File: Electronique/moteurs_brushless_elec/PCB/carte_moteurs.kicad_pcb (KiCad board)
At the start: 2 copper layers, 75 parts, among them J1 CONN_SERIAL, J2 swdio, J3 FAN, K1 Maxon-200142, K2 Maxon-200142, P1 CONN_I2C, P2 CONN_FREE, P3 CONN_CAN, P4 encoder_2, P5 encoder_1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

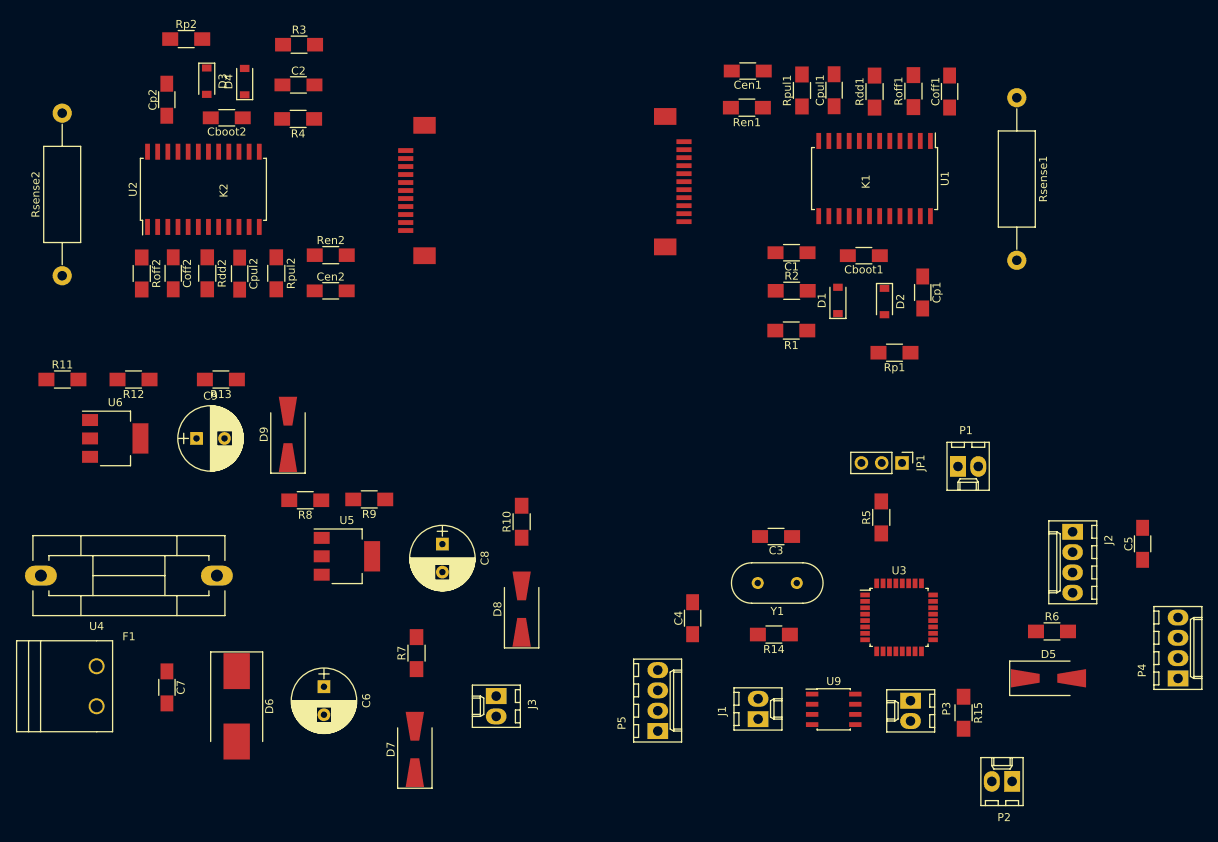
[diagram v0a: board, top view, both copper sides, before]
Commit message: debut routage brushless
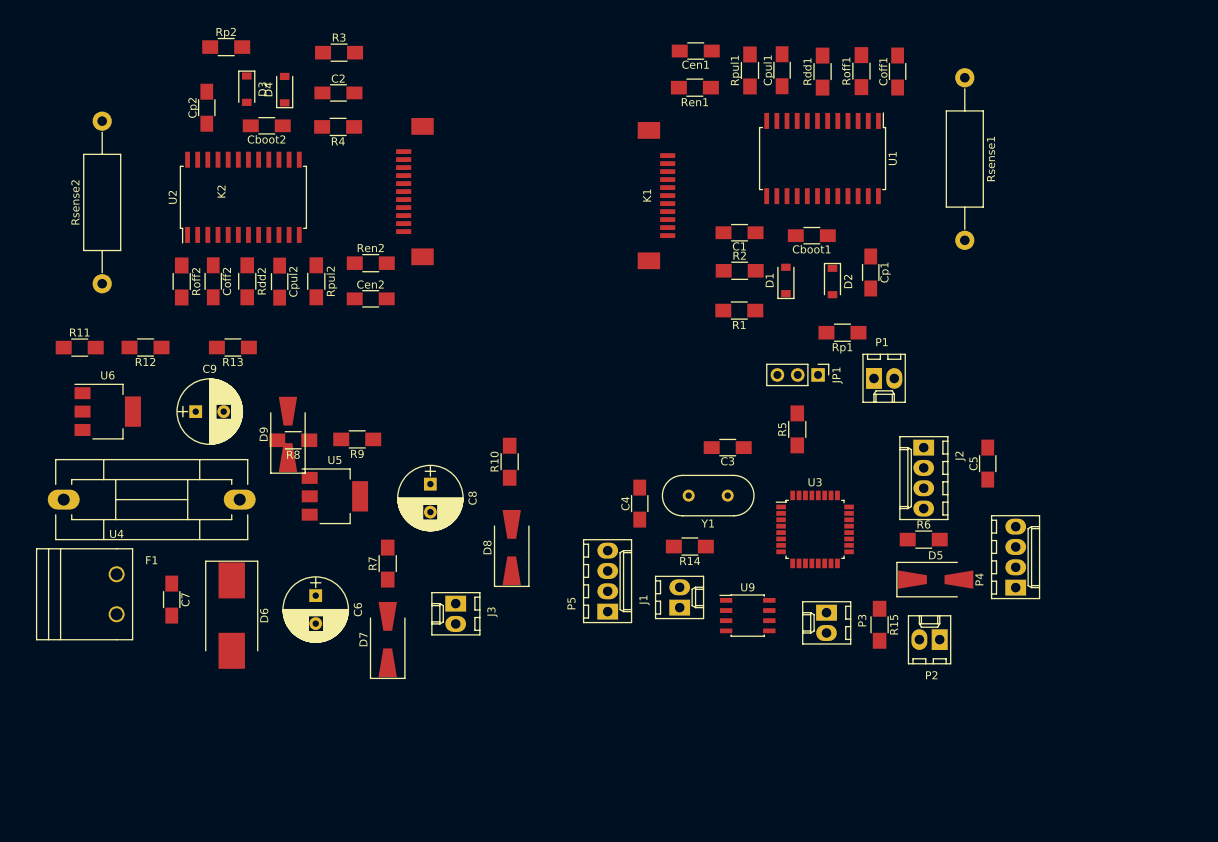
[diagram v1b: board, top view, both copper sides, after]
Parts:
- moved P4 23.3 mm to (140.5, 120.5)
- moved C5 21.8 mm to (137.0, 105.0)
- moved J2 21.4 mm to (129.0, 103.0)
- moved P2 19.9 mm to (131.0, 127.0)
- moved R6 19.7 mm to (129.0, 114.5)
- moved D5 18.7 mm to (130.5, 119.5)
- moved J1 17.0 mm to (98.5, 123.0)
- moved P5 16.2 mm to (89.5, 123.5)
- moved U9 15.9 mm to (107.0, 124.0)
- moved C4 15.8 mm to (93.5, 110.0)
- moved P1 15.2 mm to (122.8, 94.4)
- moved JP1 15.2 mm to (115.8, 93.9)
- moved P3 15.2 mm to (116.9, 123.6)
- moved R14 15.2 mm to (99.8, 115.4)
- moved R5 15.2 mm to (113.2, 100.7)
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
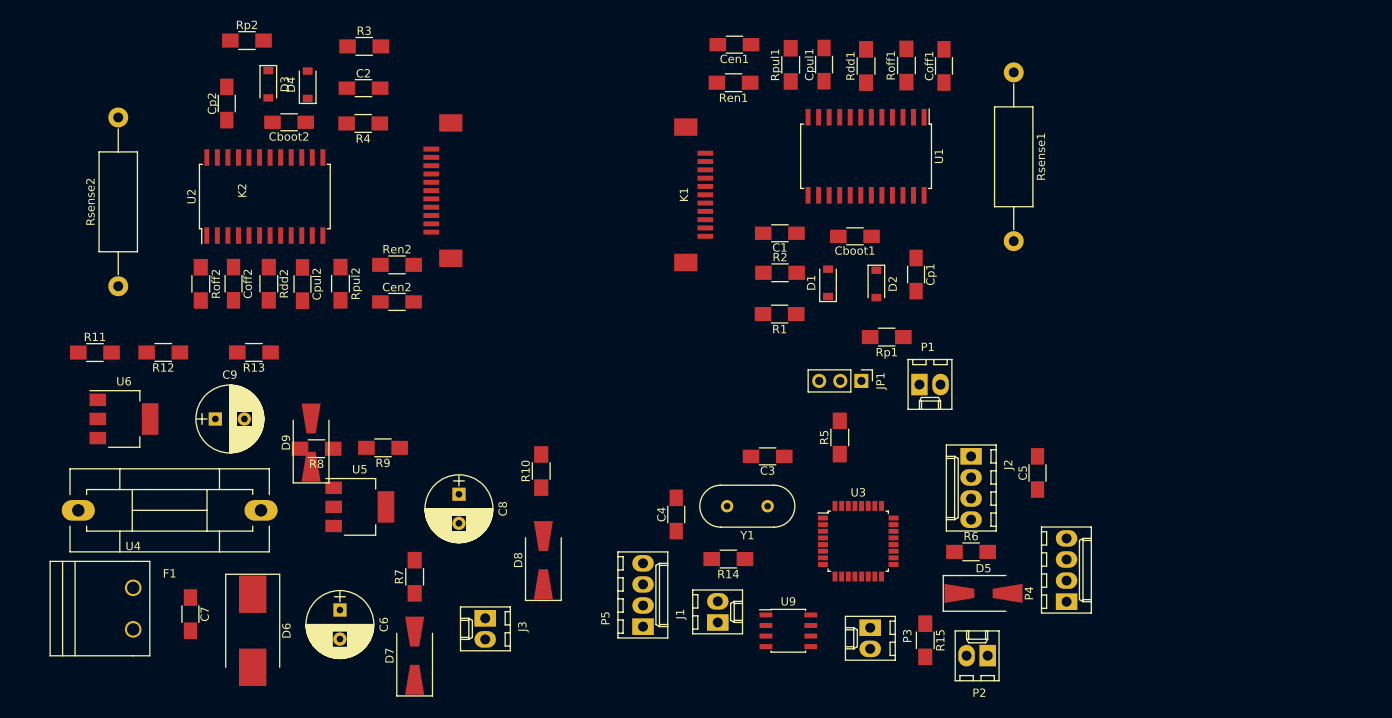
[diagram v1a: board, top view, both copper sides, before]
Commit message: placement brushless
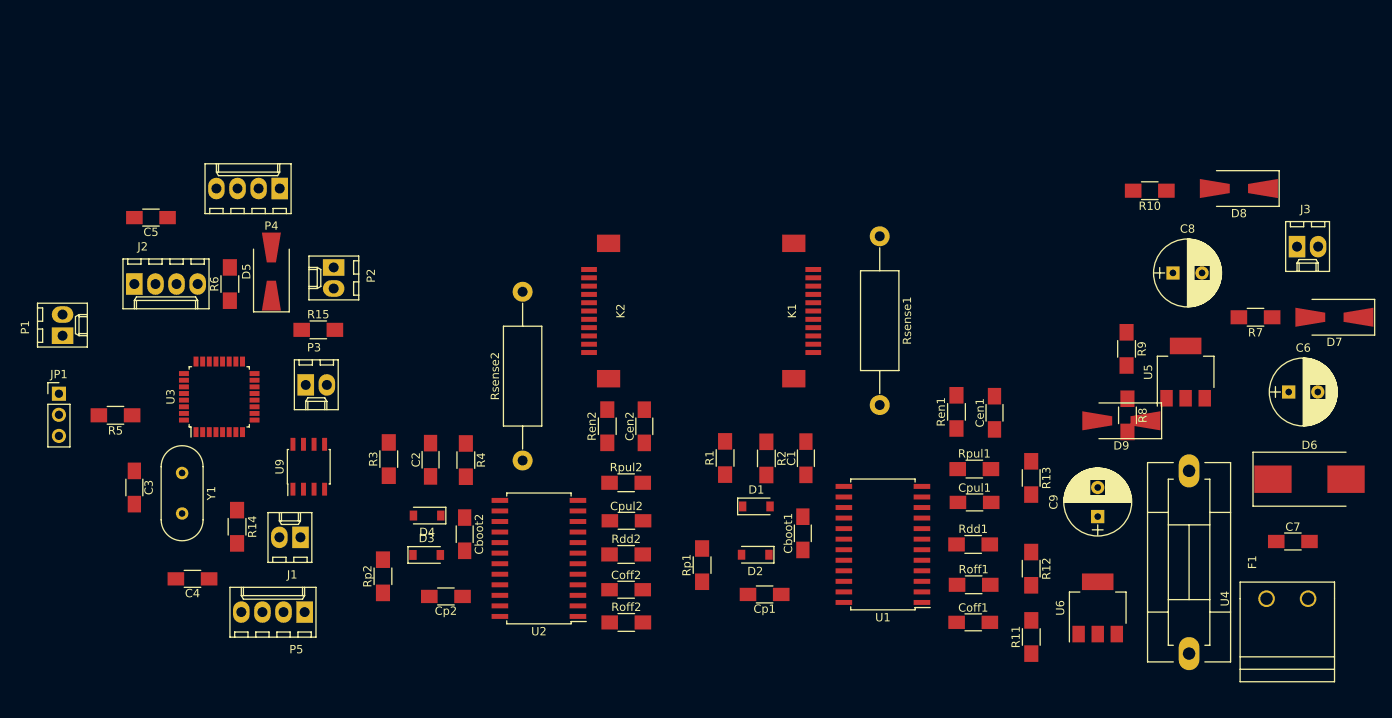
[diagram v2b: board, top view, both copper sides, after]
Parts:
- moved U4 139.0 mm to (167.1, 120.1), turned to 90 degrees
- moved C7 133.0 mm to (167.8, 113.2), turned to 0 degrees
- moved D6 128.6 mm to (169.8, 105.8), turned to 0 degrees
- moved U6 119.4 mm to (144.2, 121.2), turned to 90 degrees
- moved D7 118.0 mm to (172.8, 86.2), turned to 180 degrees
- moved R11 117.8 mm to (136.2, 124.8), turned to 90 degrees
- moved C6 117.2 mm to (167.2, 95.2), turned to 0 degrees
- moved F1 111.9 mm to (155.2, 104.8), turned to 270 degrees
- moved C5 111.1 mm to (30.2, 74.2), turned to 180 degrees
- moved R12 107.7 mm to (136.2, 116.5), turned to 270 degrees
- moved J3 107.5 mm to (168.2, 77.8), turned to 0 degrees
- moved P4 107.0 mm to (45.8, 70.8), turned to 180 degrees
- moved C9 106.9 mm to (144.2, 110.2), turned to 90 degrees
- moved R7 106.0 mm to (163.2, 86.2), turned to 180 degrees
- moved P1 103.3 mm to (19.6, 88.5), turned to 90 degrees
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
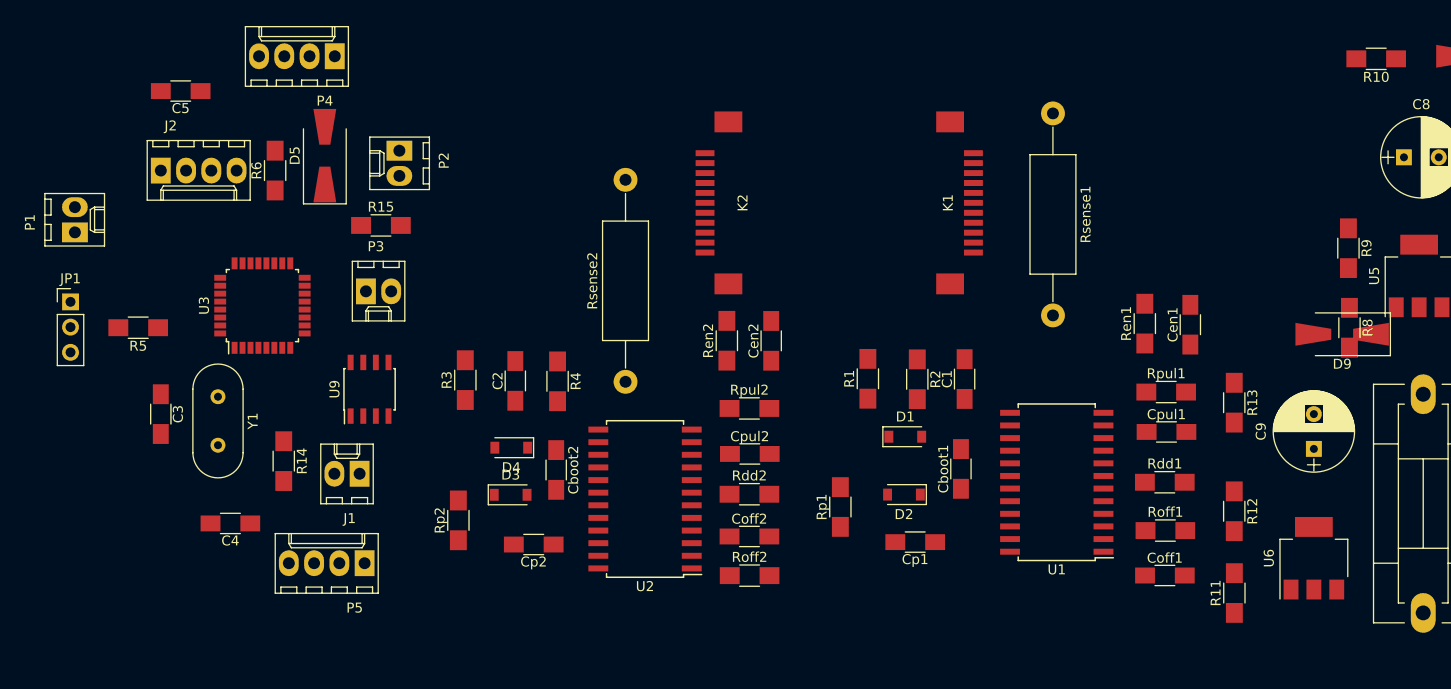
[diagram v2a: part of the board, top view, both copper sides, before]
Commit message: placement brushless
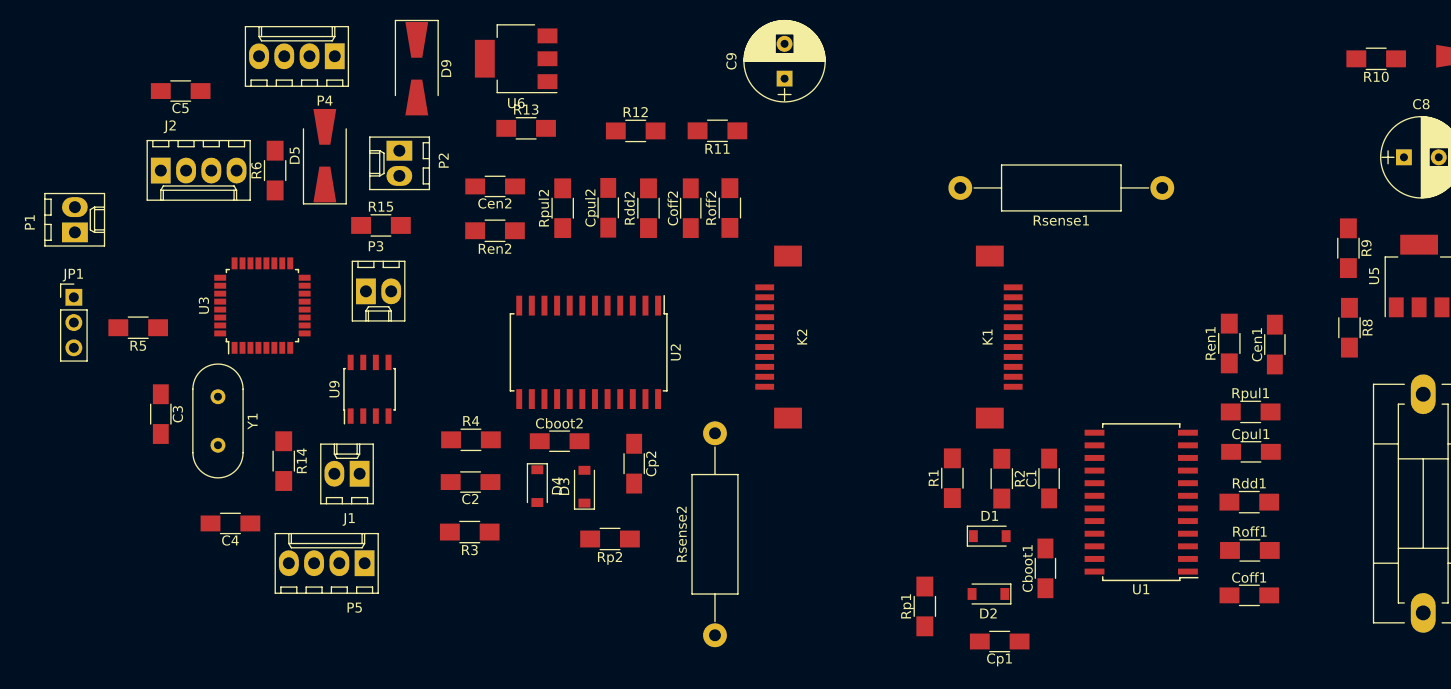
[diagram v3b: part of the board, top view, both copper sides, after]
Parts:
- moved D9 96.9 mm to (54.0, 72.0), turned to 270 degrees
- moved U6 94.7 mm to (64.0, 71.0), turned to 180 degrees
- moved R13 76.4 mm to (65.0, 78.0), turned to 0 degrees
- moved R12 71.3 mm to (76.0, 78.3), turned to 0 degrees
- moved R11 69.8 mm to (84.2, 78.2), turned to 180 degrees
- moved C9 65.0 mm to (91.0, 73.0)
- moved Roff2 37.0 mm to (85.5, 86.0), turned to 90 degrees
- moved Coff2 33.5 mm to (81.6, 86.0), turned to 90 degrees
- moved Cen2 31.8 mm to (61.9, 83.8), turned to 180 degrees
- moved Rdd2 30.5 mm to (77.3, 86.0), turned to 90 degrees
- moved Cpul2 28.6 mm to (73.3, 86.0), turned to 90 degrees
- moved Rpul2 27.5 mm to (68.7, 86.0), turned to 90 degrees
- moved Rsense2 27.0 mm to (84.0, 129.0)
- moved Ren2 25.8 mm to (61.9, 88.3), turned to 180 degrees
- moved U2 15.8 mm to (71.3, 100.5), turned to 270 degrees
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
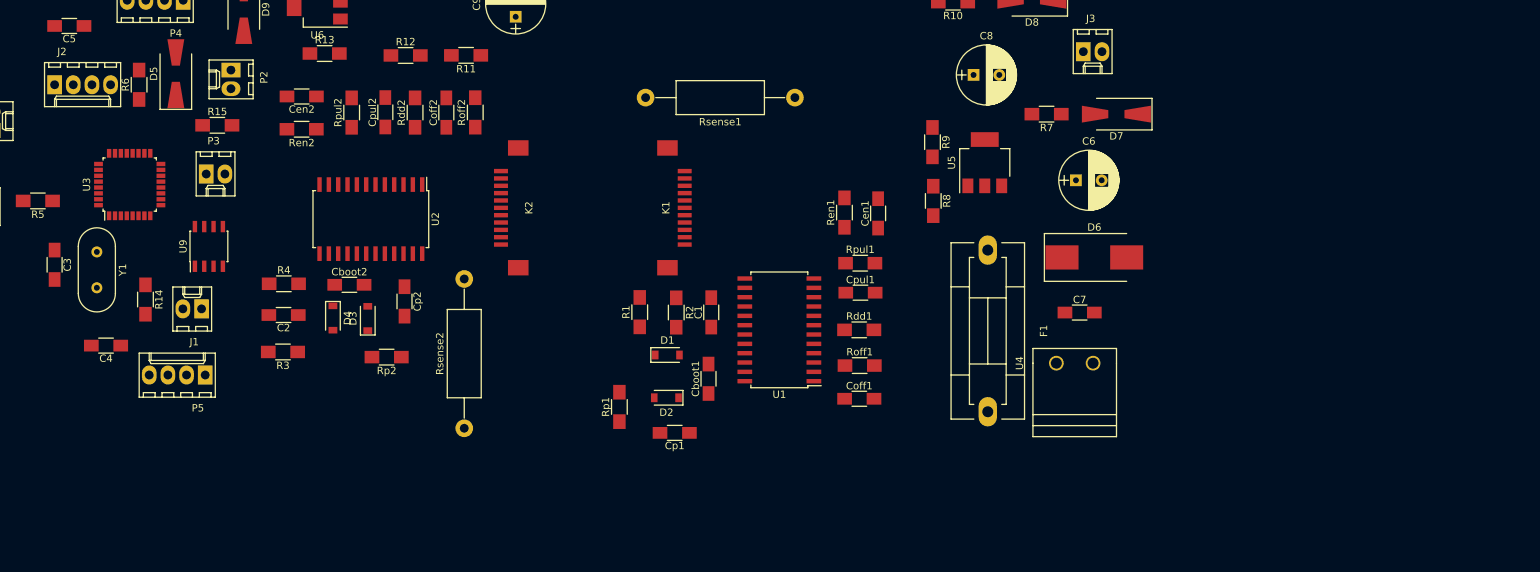
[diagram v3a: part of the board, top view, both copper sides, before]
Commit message: rectification des empreintes
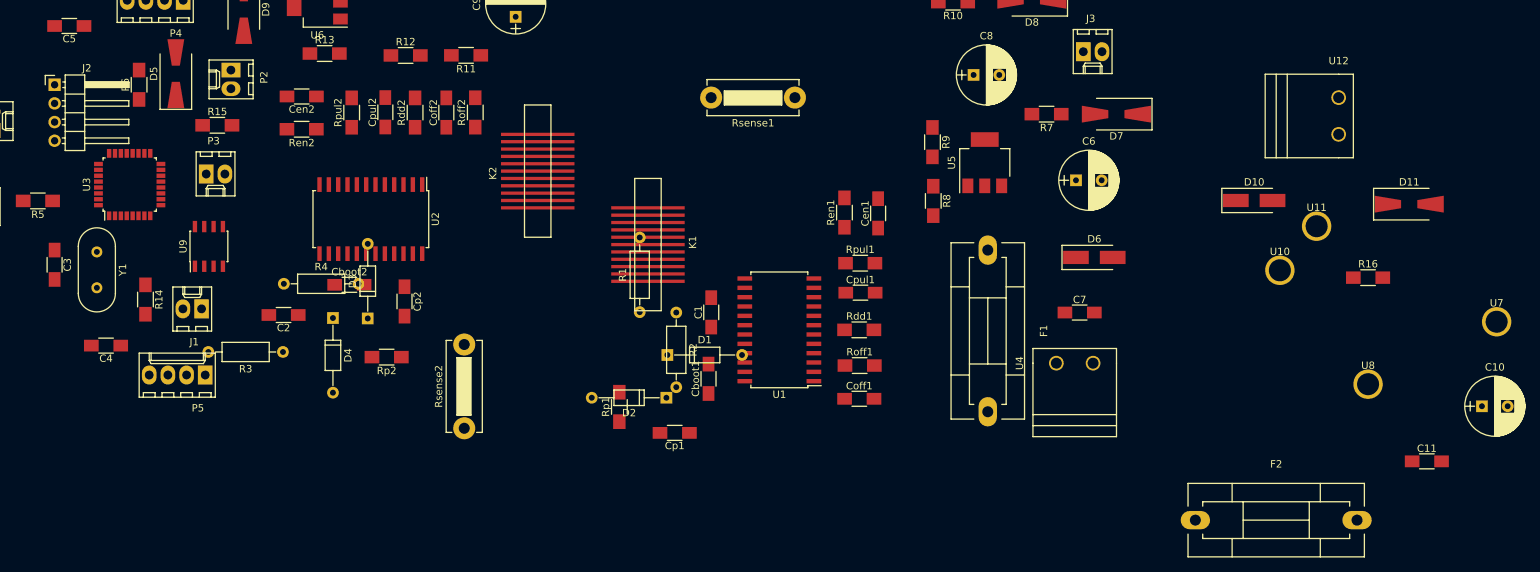
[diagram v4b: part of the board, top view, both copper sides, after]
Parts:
- added C10: 100uCP, Capacitors_THT:CP_Radial_D8.0mm_P3.50mm, F.Cu at (222.5, 126.0)
- added C11: 100nC, Capacitors_SMD:C_1206_HandSoldering, F.Cu at (215.0, 133.5)
- added D10: D_10A, Diodes_SMD:D_SMA_Handsoldering, F.Cu at (191.5, 98.0)
- added D11: LED_ALT, Diodes_SMD:D_SMA-SMB_Universal_Handsoldering, F.Cu at (212.6, 98.5)
- added F2: Fuse, Fuse_Holders_and_Fuses:Fuseholder5x20_horiz_SemiClosed_Casing10x25mm, F.Cu at (183.5, 141.5)
- added R16: R, Resistors_SMD:R_1206_HandSoldering, F.Cu at (207.0, 108.5)
- added U10: Trou-3, maxon:Trou-3, F.Cu at (195.0, 107.5)
- added U11: Trou-3, maxon:Trou-3, F.Cu at (200.0, 101.5)
- added U12: B_Plug_5mm, B plug:B plug 5mm, F.Cu at (203.0, 86.5)
- added U7: Trou-3, maxon:Trou-3, F.Cu at (224.5, 114.5)
- added U8: Trou-3, maxon:Trou-3, F.Cu at (207.0, 123.0)
- D1, D2, D3, D4: footprint Diodes_SMD:D_SOD-123 -> Diodes_THT:D_DO-35_SOD27_P10.16mm_Horizontal
- D6: footprint Diodes_SMD:D_SMC_Handsoldering -> Diodes_SMD:D_SMA_Handsoldering
- J2: footprint Connectors_Molex:Molex_KK-6410-04_04x2.54mm_Straight -> Pin_Headers:Pin_Header_Angled_1x04_Pitch2.54mm
- K1, K2: footprint maxon:Molex-52207-0433 -> maxon:Molex-52610-1133
- R1, R2, R3, R4: footprint Resistors_SMD:R_1206_HandSoldering -> Resistors_THT:R_Axial_DIN0207_L6.3mm_D2.5mm_P10.16mm_Horizontal
- Rsense1, Rsense2: footprint Resistors_THT:R_Axial_DIN0414_L11.9mm_D4.5mm_P20.32mm_Horizontal -> Resistors_THT:R_Bare_Metal_Element_L12.4mm_W4.8mm_P11.40mm
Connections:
- Cboot2 pad 2: VCC -> VDD
- D3 pad 2: VCC -> VDD
- U2 pad 17: VCC -> VDD
- U2 pad 20: VCC -> VDD

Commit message: trous et dim ok
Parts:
- K1, K2: moved to B.Cu
- moved R8 194.7 mm to (-46.0, 79.5)
- moved U5 194.7 mm to (-39.0, 74.2)
- moved R9 194.7 mm to (-46.1, 71.5)
- moved U7 172.7 mm to (53.0, 135.0)
- moved Cp1 158.2 mm to (24.6, -1.87)
- moved R3 144.2 mm to (-41.1, 15.2)
- moved U10 143.1 mm to (53.0, 90.0)
- moved C2 128.6 mm to (56.9, -15.0)
- moved Cboot2 128.6 mm to (65.8, -19.1)
- moved Cp2 128.6 mm to (73.3, -16.8)
- moved D3 128.6 mm to (68.3, -14.5)
- moved D4 128.6 mm to (63.6, -14.6)
- moved R4 128.6 mm to (56.9, -19.2)
- moved Rp2 128.6 mm to (70.9, -9.24)
- moved Rdd2 110.5 mm to (-8.05, 15.9)
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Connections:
- F2 pad 2: GND -> Net-(F2-Pad2)
- U12 pad 1: Net-(U12-Pad1) -> Net-(F2-Pad2)
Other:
- board outline added: 154 x 65 mm
- net class Default: clearance 0.25 -> 0.3; trace_width 0.5 -> 0.508; via_dia 1.2 -> 1.3
- net class Power added: clearance 0.3, trace_width 3, via_dia 1.3, via_drill 0.8
- rule trace_clearance: 0.25 -> 0.3
